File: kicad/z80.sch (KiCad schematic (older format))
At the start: 18 parts, among them J3 Conn_02x20_Odd_Even, U1 Z80CPU, U23 74AC273, U3 SST39SF010, U4 74AHC32, U5 AS6C1008-55PCN, U6 74HC154, U9 74AHC02, X1 ACH10MHZ

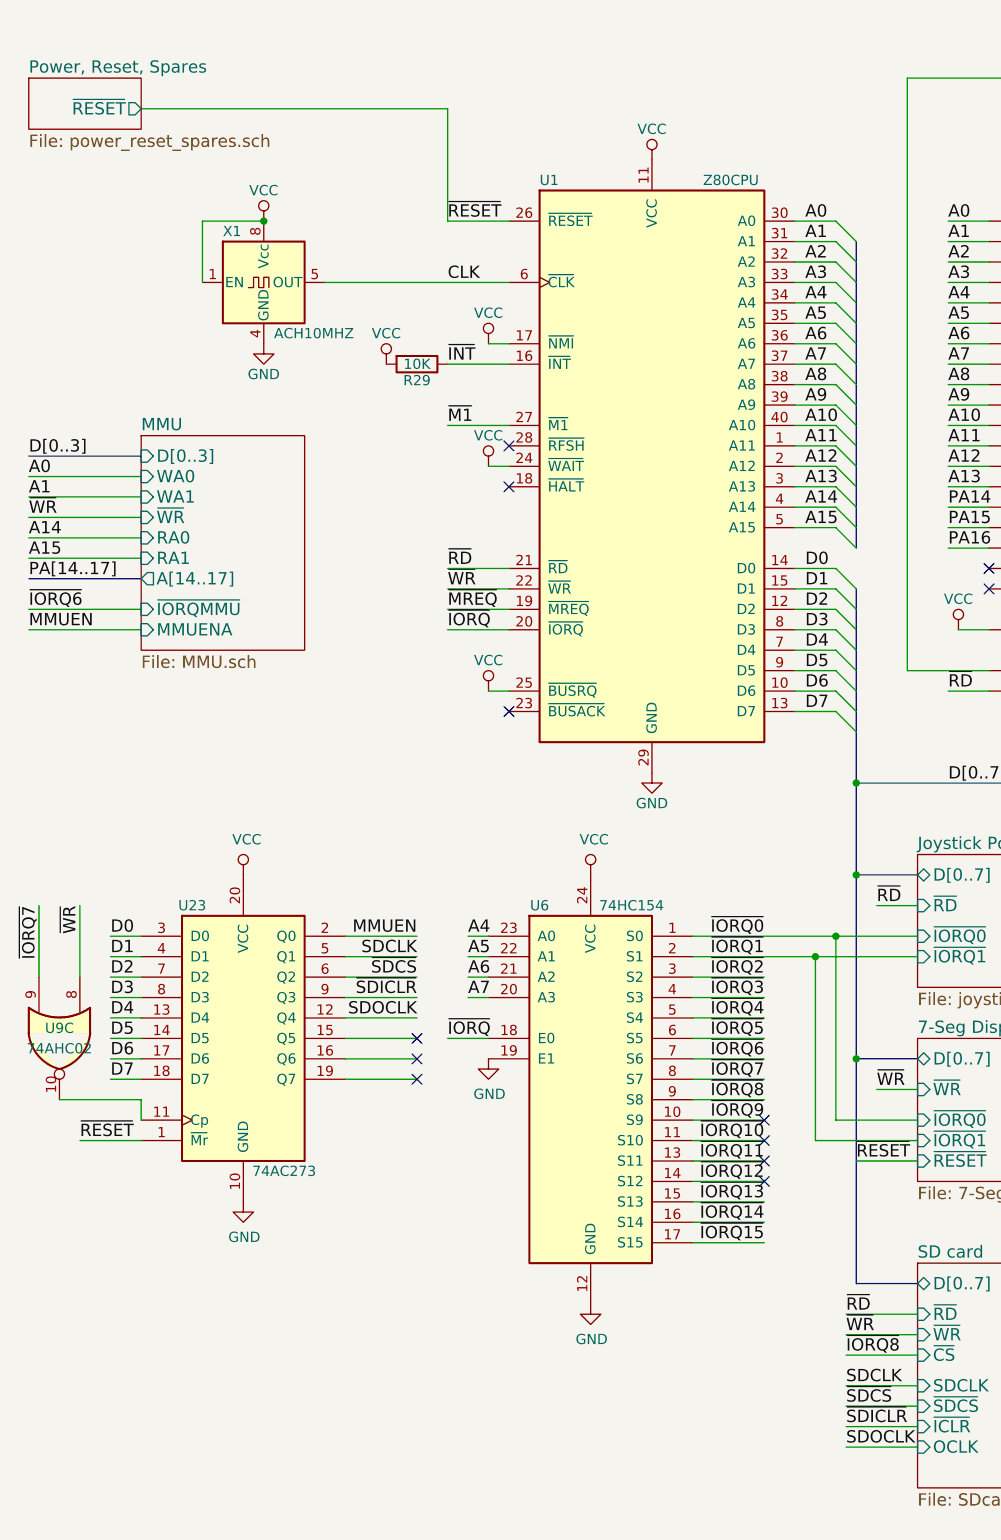
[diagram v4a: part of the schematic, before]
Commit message: Add audio output.
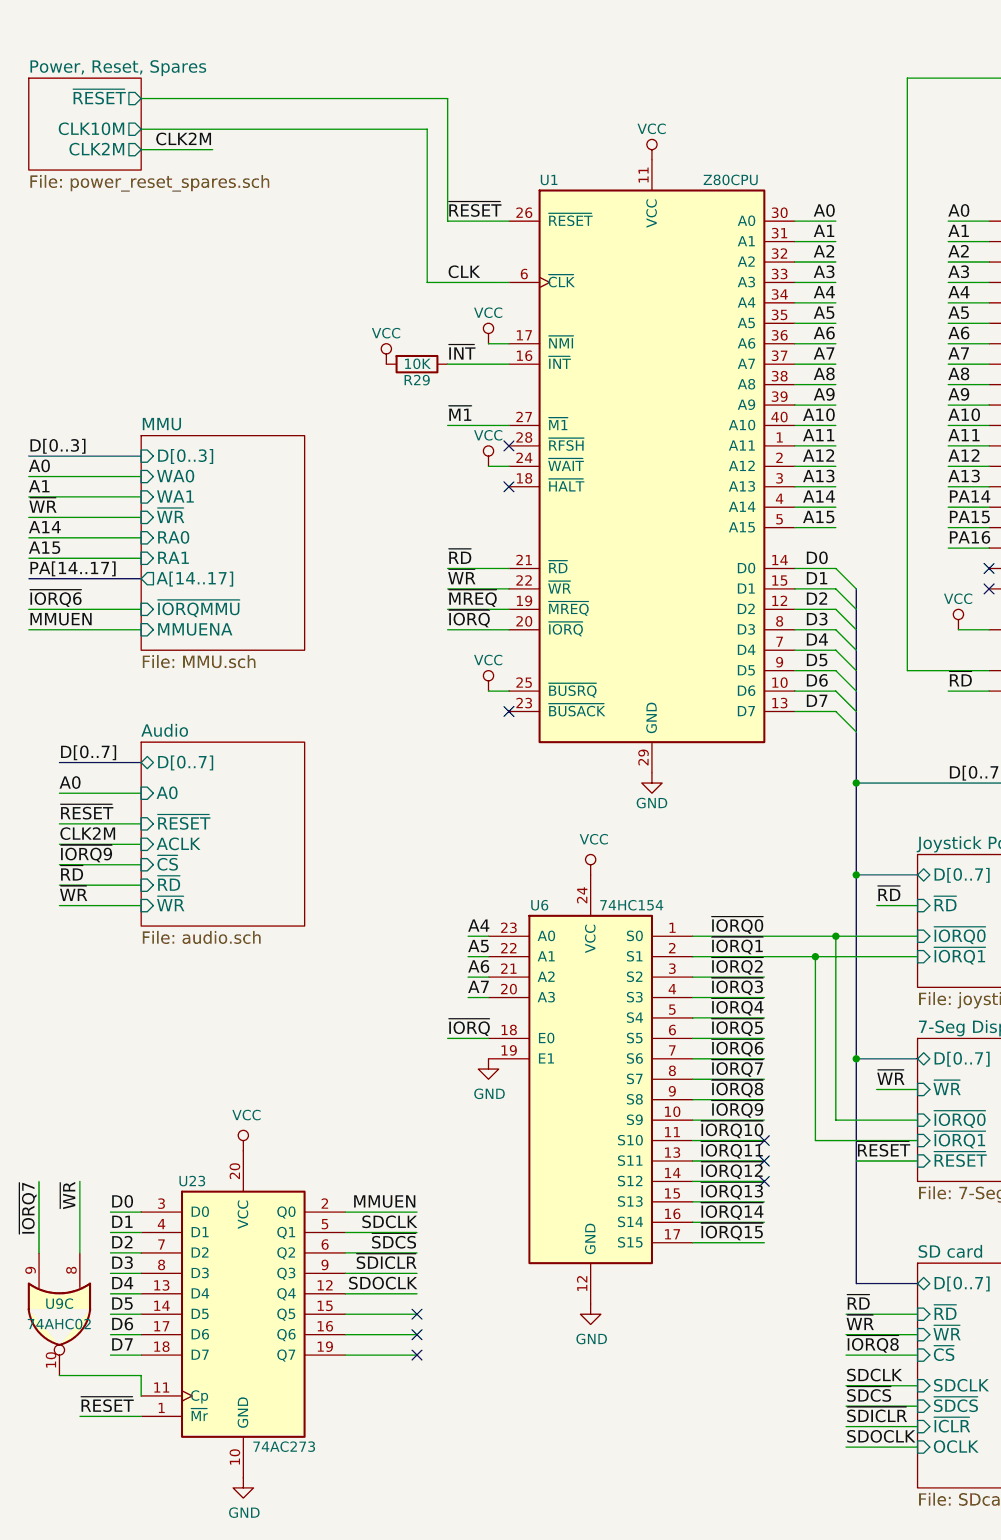
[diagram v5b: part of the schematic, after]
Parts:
- removed X1: ACH10MHZ, Oscillators:Oscillator_DIP-8, symbol Oscillator:CXO_DIP8
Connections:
- no-connect marks 18 -> 17
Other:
- moved on the sheet: U23, U9C
